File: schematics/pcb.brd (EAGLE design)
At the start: 86.3 x 110.2 mm, 39 parts, among them IC1 7805TV, IC2 4050D, IC3 LP298XS, Q1 16Mhz, Q2 16Mhz, X1 MICROSD

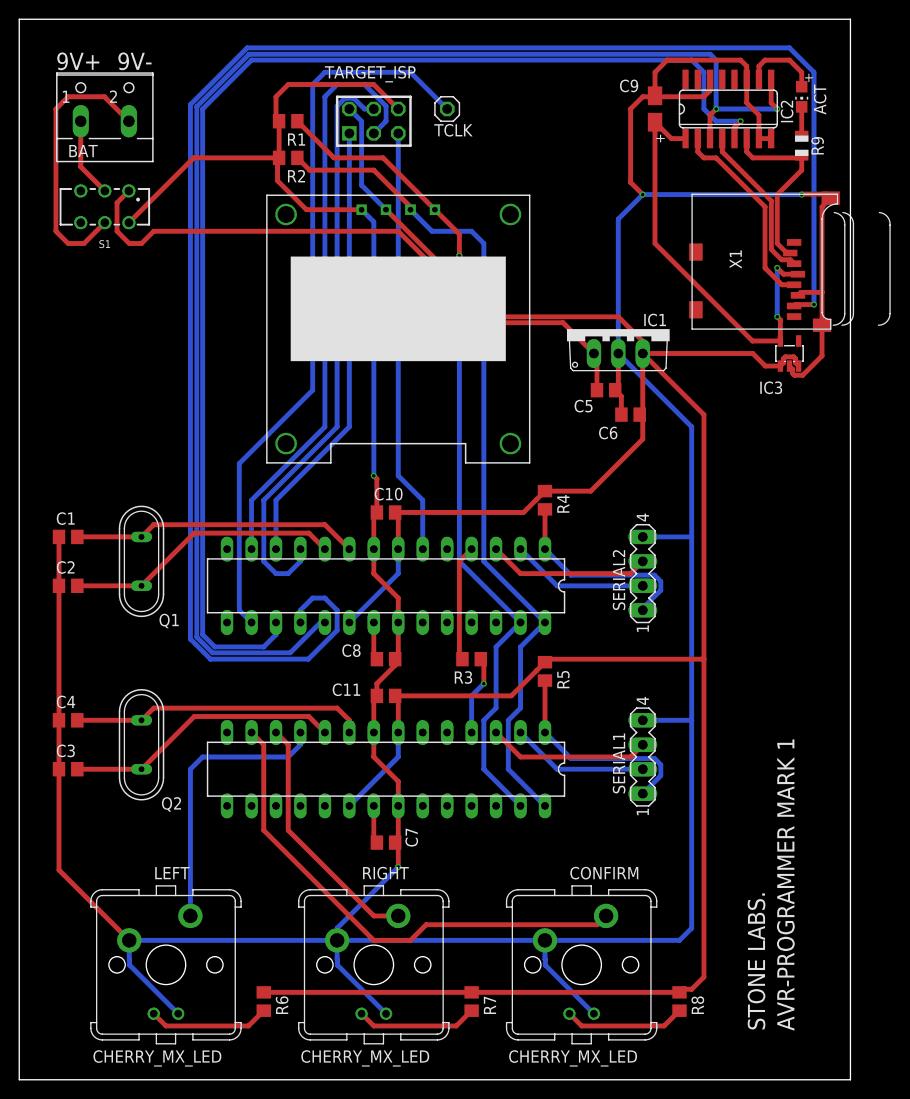
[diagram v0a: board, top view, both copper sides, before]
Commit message: PLaced images on PCB
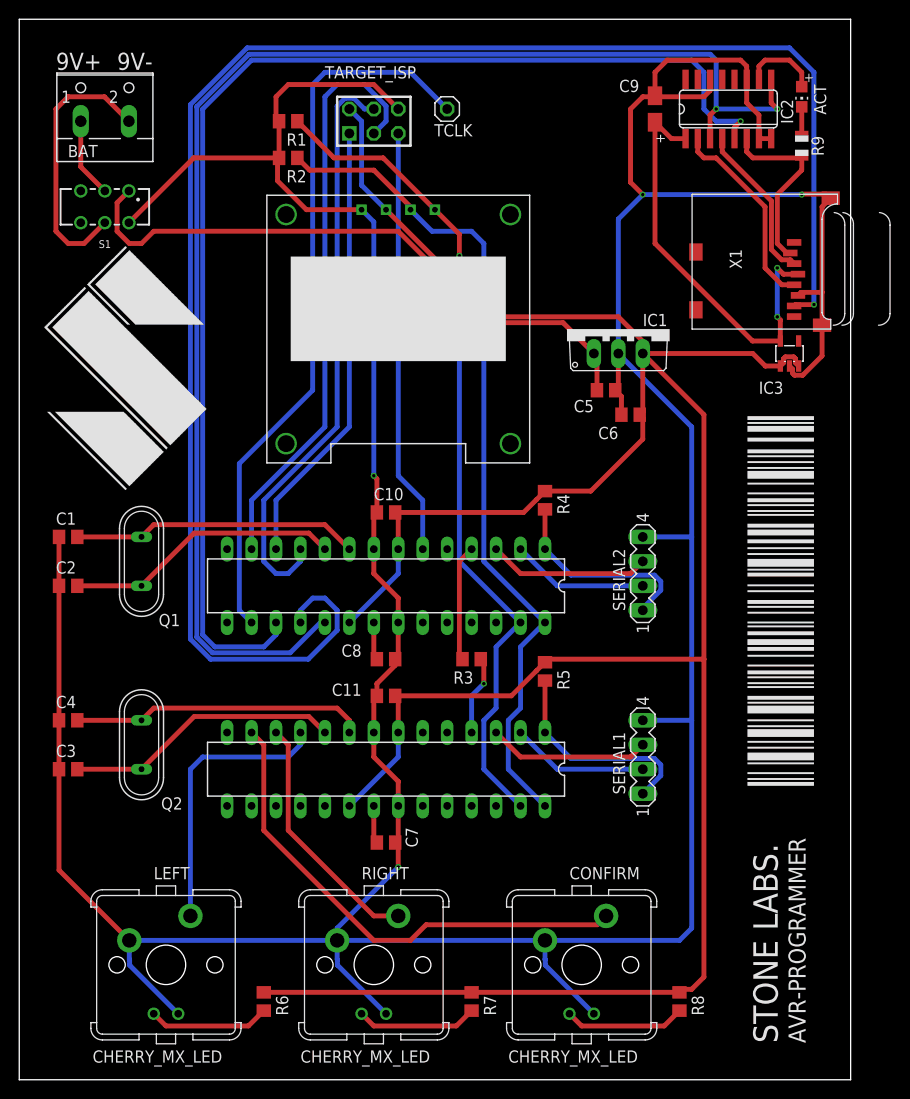
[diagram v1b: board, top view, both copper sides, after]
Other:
- board size 86.3 x 110.2 mm -> 86.4 x 110.2 mm
- board text added: "AVR-PROGRAMMER"
- board text removed: "AVR-PROGRAMMER MARK 1"
